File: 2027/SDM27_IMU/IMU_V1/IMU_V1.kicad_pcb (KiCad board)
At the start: 2 copper layers, 80 parts, among them IC3 ISM330DHCXTR, IC7 IIS2MDCTR, J1 WEIPU SA12 7PIN, J3 USB_C_Receptacle_USB2.0_16P, U2 ESP32-C5HR8, U3 TPS2121RUXR, U4 TPS62901RPJR, U5 SST26VF064B-104I_SM, U6 TLP175A_TPL,E, U7 USBLC6-2SC6, U8 TCAN3403DRBRQ1, Y3 CX1612DB48000D0FPJC1

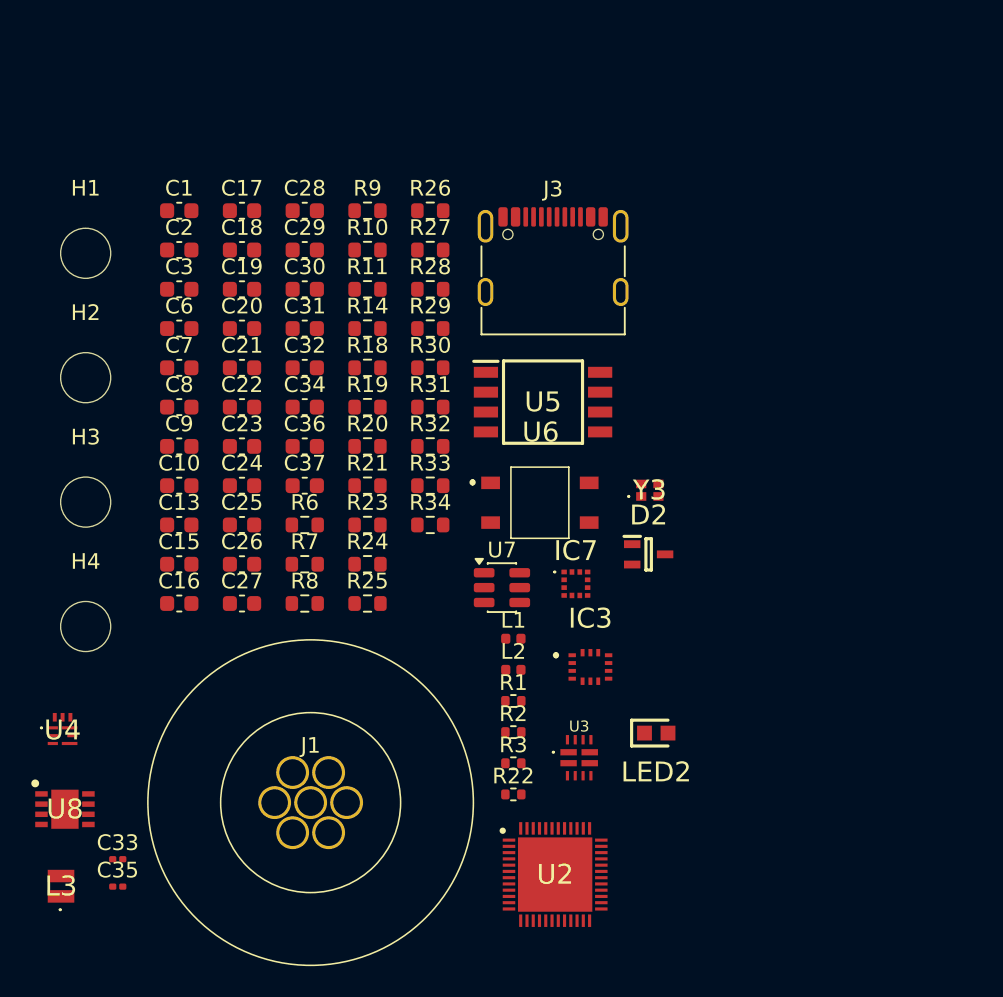
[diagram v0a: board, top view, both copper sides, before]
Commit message: IMU V1 Fixes
redesignated resistor and capacitor values to be sorted.
Added 7 pin jst-ph to board
Removed extra pair of resistors on USB D Pins that was added. (Already had a set on MCU)
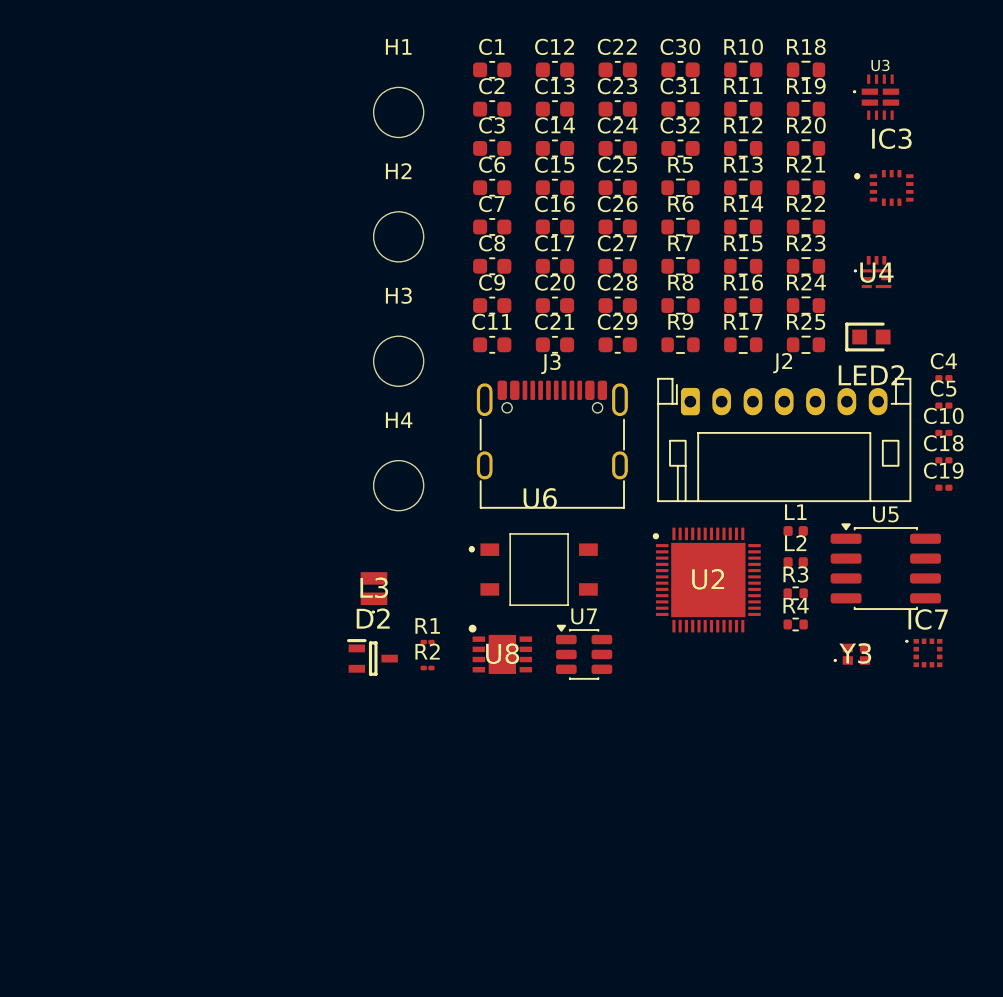
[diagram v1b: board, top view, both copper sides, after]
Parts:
- removed C33, C35: 12pF, Capacitor_SMD:C_0201_0603Metric
- removed C34, C36, C37: 100nF, Capacitor_SMD:C_0603_1608Metric
- removed J1: WEIPU SA12 7PIN, SDM Footprints:SA12 7Pin
- removed R26: 18.2k, Resistor_SMD:R_0603_1608Metric
- removed R27: 10.2k, Resistor_SMD:R_0603_1608Metric
- removed R28: 100k, Resistor_SMD:R_0603_1608Metric
- removed R29: 113k, Resistor_SMD:R_0603_1608Metric
- removed R30: 24.9k, Resistor_SMD:R_0603_1608Metric
- removed R31: 330, Resistor_SMD:R_0603_1608Metric
- removed R32, R33: 2.2k, Resistor_SMD:R_0603_1608Metric
- removed R34: 120, Resistor_SMD:R_0603_1608Metric
- added C11: 10uF, Capacitor_SMD:C_0603_1608Metric, F.Cu at (127.5, 93.8)
- added C12: 10uF, Capacitor_SMD:C_0603_1608Metric, F.Cu at (131.5, 76.3)
- added C14: 0.3pF, Capacitor_SMD:C_0603_1608Metric, F.Cu at (131.5, 81.3)
- added C4: 1uF, Capacitor_SMD:C_0201_0603Metric, F.Cu at (156.3, 96.0)
- added C5: 1uF, Capacitor_SMD:C_0201_0603Metric, F.Cu at (156.3, 97.7)
- added J2: Conn_01x07_Pin, Connector_JST:JST_PH_S7B-PH-K_1x07_P2.00mm_Horizontal, F.Cu at (140.1, 97.5)
- added R12: 18.2k, Resistor_SMD:R_0603_1608Metric, F.Cu at (143.5, 81.3)
- added R13: 5k, Resistor_SMD:R_0603_1608Metric, F.Cu at (143.5, 83.8)
- added R15: 23.7k, Resistor_SMD:R_0603_1608Metric, F.Cu at (143.5, 88.8)
- added R16: 10.2k, Resistor_SMD:R_0603_1608Metric, F.Cu at (143.5, 91.3)
- added R17: 5k, Resistor_SMD:R_0603_1608Metric, F.Cu at (143.5, 93.8)
- added R4: 27, Resistor_SMD:R_0402_1005Metric, F.Cu at (146.8, 111.7)
- added R5: 2.2k, Resistor_SMD:R_0603_1608Metric, F.Cu at (139.5, 83.8)
- C10: value 10uF -> 100nF; footprint Capacitor_SMD:C_0603_1608Metric -> Capacitor_SMD:C_0201_0603Metric
- C13: value 0.3pF -> 10uF
- C15: value 220nF -> 0.8pF
- C16: value 10uF -> 2.6pF
- C17: value 100nF -> 3pF
- C18, C19: value 100nF -> 12pF; footprint Capacitor_SMD:C_0603_1608Metric -> Capacitor_SMD:C_0201_0603Metric
- C20: value 1uF 10V 0603 -> 100nF
- C21: value 10uF 25V -> 100nF
- C22: value 10nF -> 100nF
- C23: value 22uF -> 100nF
- C24: value 0.8pF -> 100nF
- C25: value 10uF -> 1uF 10V 0603
- C26: value 100nF -> 10uF 25V
- C27: value 100nF -> 10nF
- C28: value 3pF -> 22uF
- C29: value 100nF -> 220nF
- C30: value 2.6pF -> 10uF
- C32: value 10uF -> 100nF
- C7, C8: value 1uF -> 100nF
- R1, R2: footprint Resistor_SMD:R_0402_1005Metric -> Resistor_SMD:R_01005_0402Metric
- R10: value 27 -> 100
- R11: value 27 -> 63.4k
- R14: value 63.4k -> 5k
- R18: value 10k -> 5k
- R19: value 2.2k -> 100k
- R20: value 2.2k -> 113k
- R21: value 5.1k -> 24.9k
- R22: value 27 -> 330; footprint Resistor_SMD:R_0402_1005Metric -> Resistor_SMD:R_0603_1608Metric
- R23: value 5.1k -> 10k
- R24: value 23.7k -> 2.2k
- R25: value 5k -> 2.2k
- R6: value 10k -> 2.2k
- R7: value 5k -> 10k
- R8, R9: value 5k -> 5.1k
- U5: value SST26VF064B-104I_SM -> GD25Q32ESIG; footprint SDM Footprints:SOIC127P794X203-8N -> Package_SO:SOP-8_3.76x4.96mm_P1.27mm
- moved U4 59.6 mm to (152.0, 89.3)
- moved C10 49.0 mm to (156.3, 99.5)
- moved C18 46.8 mm to (156.3, 101.2)
- moved C19 46.6 mm to (156.3, 103.0)
- moved U3 46.4 mm to (152.3, 78.0)
- moved R22 40.8 mm to (147.5, 86.3)
- moved IC3 36.2 mm to (153.0, 83.8)
- moved C13 35.8 mm to (131.5, 78.8)
- moved C15 34.0 mm to (131.5, 83.8)
- moved C16 34.0 mm to (131.5, 86.3)
- moved R18 33.9 mm to (147.5, 76.3)
- moved R19 33.9 mm to (147.5, 78.8)
- moved R21 33.9 mm to (147.5, 83.8)
- moved R20 33.9 mm to (147.5, 81.3)
- moved R24 32.5 mm to (147.5, 91.3)
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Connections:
- C10 pad 1: +3.3V -> /VDD_SPI
- C15 pad 1: Net-(IC7-C1) -> +3.3V
- C16 pad 1: +3.3V -> Net-(U2-VDDA1)
- C18 pad 1: +3.3V -> Net-(C18-Pad1)
- C18 pad 2: GND -> Net-(C18-Pad2)
- C19 pad 1: GND -> Net-(U2-XTAL_N)
- C19 pad 2: VBUS -> Net-(C19-Pad2)
- C20 pad 1: Net-(U3-SS) -> GND
- C20 pad 2: GND -> +3.3V
- C21 pad 1: VCC -> GND
- C21 pad 2: GND -> +3.3V
- C22 pad 1: Net-(U4-SS/TR) -> GND
- C22 pad 2: GND -> VBUS
- C25 pad 1: +3.3V -> Net-(U3-SS)
- C26 pad 1: +3.3V -> VCC
- C27 pad 1: +3.3V -> Net-(U4-SS/TR)
- C29 pad 1: +3.3V -> Net-(IC7-C1)
- C30 pad 1: Net-(U2-VDDA1) -> +3.3V
- C6 pad 1: GND -> +3.3V
- C6 pad 2: +3.3V -> GND
- C7 pad 1: /CHIP_PU -> +3.3V
- C8 pad 1: Net-(U2-BOOT) -> +3.3V
- C9 pad 1: GND -> +3.3V
- C9 pad 2: +3.3V -> GND
- IC3 pad 12: Net-(IC3-CS) -> /I_CS
- IC7 pad 3: Net-(IC7-CS) -> /M_CS
- J3 pad A12: unconnected-(J3-GND-PadA12) -> GND
- J3 pad B1: unconnected-(J3-GND-PadB1) -> GND
- J3 pad B12: unconnected-(J3-GND-PadB12) -> GND
- L1 pad 2: Net-(C33-Pad1) -> Net-(C18-Pad1)
- R10 pad 1: /USB_D+ -> Net-(R10-Pad1)
- R10 pad 2: Net-(R10-Pad2) -> /CAN+
- R11 pad 1: /USB_D- -> Net-(U3-OV1)
- R11 pad 2: Net-(R11-Pad2) -> +12V
- R14 pad 1: Net-(U3-OV1) -> GND
- R14 pad 2: +12V -> Net-(U3-OV1)
- R18 pad 1: +3.3V -> GND
- R18 pad 2: Net-(IC7-CS) -> Net-(U3-OV2)
- R19 pad 1: /SDX -> GND
- R19 pad 2: +3.3V -> Net-(U3-ILIM)
- R20 pad 2: /SCX -> Net-(U4-VSET)
- R21 pad 1: Net-(J3-CC1) -> Net-(U4-VSET)
- R22 pad 1: /USB_D- -> +3.3V
- R22 pad 2: Net-(U2-GPIO13) -> /PWR_LED
- R23 pad 1: Net-(J3-CC2) -> +3.3V
- R23 pad 2: GND -> /M_CS
- R24 pad 1: Net-(U3-OV2) -> /SDX
- R24 pad 2: VBUS -> +3.3V
- R25 pad 1: GND -> +3.3V
- R25 pad 2: Net-(U3-OV2) -> /SCX
- R6 pad 1: Net-(IC3-CS) -> /I2C1_SCL
- R7 pad 1: GND -> /I_CS
- R7 pad 2: Net-(U3-PR1) -> +3.3V
- R8 pad 1: GND -> Net-(J3-CC1)
- R8 pad 2: Net-(U3-OV1) -> GND
- R9 pad 1: GND -> Net-(J3-CC2)
- R9 pad 2: Net-(U3-CP2) -> GND
- U2 pad 10: unconnected-(U2-GPIO1-Pad10) -> /I_CS
- U2 pad 11: unconnected-(U2-GPIO2-Pad11) -> /M_CS
- U6 pad 6: Net-(R34-Pad1) -> Net-(R10-Pad1)
- U7 pad 1: Net-(R10-Pad2) -> /USB_D+
- U7 pad 3: Net-(R11-Pad2) -> /USB_D-
- Y3 pad 1: Net-(C33-Pad2) -> Net-(C18-Pad2)
- Y3 pad 3: Net-(C35-Pad2) -> Net-(C19-Pad2)

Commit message: port to pc
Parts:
- removed J2: Conn_01x07_Pin, Connector_JST:JST_PH_S7B-PH-K_1x07_P2.00mm_Horizontal
- added J1: WEIPU SA12 7PIN, Connector_JST:JST_PH_B7B-PH-K_1x07_P2.00mm_Vertical, F.Cu at (145.0, 151.5)
- added SW1: SW_Push, Button_Switch_SMD:SW_SPST_CK_KXT3, F.Cu at (131.0, 161.5)
- added SW2: SW_Push, Button_Switch_SMD:SW_SPST_CK_KXT3, F.Cu at (131.0, 166.0)
- moved H1 86.9 mm to (178.0, 145.0)
- moved H2 82.7 mm to (168.5, 155.0)
- moved U3 73.7 mm to (101.5, 131.5), turned to -90 degrees
- moved L1 63.5 mm to (207.0, 85.2)
- moved L2 63.5 mm to (207.0, 87.2)
- moved R3 63.5 mm to (207.0, 89.2)
- moved R4 63.5 mm to (207.0, 91.2)
- moved H4 63.2 mm to (169.0, 144.5)
- moved U4 61.7 mm to (107.1, 131.8), turned to 180 degrees
- moved H3 61.5 mm to (168.5, 134.5)
- moved LED2 60.7 mm to (107.5, 135.0)
- moved R1 58.7 mm to (178.8, 93.5)
- moved R2 58.7 mm to (178.8, 95.2)
- moved C1 56.0 mm to (183.5, 77.3)
- moved C11 56.0 mm to (183.5, 94.8)
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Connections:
- net /CHIP_PU renamed /CP
- net Net-(U2-BOOT) renamed /BOOT
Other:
- board outline added: 52 x 41 mm
- copper layers 2 -> 4
- board text added: "BUCK"
- board text added: "CAN D2"
- board text added: "CRY"
- board text added: "ESD (U7)"
- board text added: "ESP-C5"
- board text added: "FLASH"
- board text added: "IMU"
- board text added: "JST"
- board text added: "LED"
- board text added: "MAG"
- board text added: "MUX"
- board text added: "OPTO"
- board text added: "Switch"
- board text added: "TCAN"
- board text added: "USB"
- board text added: "temp"

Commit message: IMU PCB V1
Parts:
- C1, C12, C16, C17, C18, C19, C2, C7, C8, J3, L1, L2, Y3: moved to B.Cu
- moved H1 85.0 mm to (115.0, 88.0)
- moved R3 81.8 mm to (126.5, 104.0), turned to 180 degrees
- moved R4 81.2 mm to (126.5, 102.1)
- moved R18 76.8 mm to (131.7, 104.5), turned to -90 degrees
- moved R9 76.4 mm to (121.5, 114.0), turned to 180 degrees
- moved R11 76.2 mm to (129.7, 110.5), turned to -90 degrees
- moved C22 76.1 mm to (123.0, 110.5)
- moved R12 73.9 mm to (131.2, 110.5), turned to -90 degrees
- moved R8 73.7 mm to (125.0, 114.0)
- moved L2 73.3 mm to (134.6, 98.9), turned to 90 degrees
- moved R14 72.6 mm to (129.7, 107.5), turned to -90 degrees
- moved R19 72.0 mm to (137.7, 109.0), turned to 90 degrees
- moved R13 71.9 mm to (131.2, 107.5), turned to -90 degrees
- moved C10 71.6 mm to (130.1, 94.3), turned to 180 degrees
- moved SW1 69.4 mm to (115.0, 94.0)
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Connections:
- U2 pad 10: /I_CS -> unconnected-(U2-GPIO1-Pad10)
- U2 pad 11: /M_CS -> unconnected-(U2-GPIO2-Pad11)
- U2 pad 13: unconnected-(U2-GPIO4-Pad13) -> /CAN_CTX
- U2 pad 14: unconnected-(U2-GPIO5-Pad14) -> /CAN_RTX
- U2 pad 16: unconnected-(U2-GPIO7-Pad16) -> /M_CS
- U2 pad 19: /CAN_TERM -> /I_CS
- U2 pad 20: unconnected-(U2-GPIO11-Pad20) -> /INT
- U2 pad 33: /CAN_CTX -> unconnected-(U2-GPIO23-Pad33)
- U2 pad 34: /CAN_RTX -> unconnected-(U2-GPIO24-Pad34)
- U2 pad 9: /INT -> unconnected-(U2-GPIO0-Pad9)
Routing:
- net GND: track 0.00 -> 90.5 mm, vias 0 -> 26
- net +3.3V: track 0.00 -> 52.0 mm, vias 0 -> 17
- net /CP: track 0.00 -> 41.2 mm, vias 0 -> 2
- net VBUS: track 0.00 -> 32.2 mm, vias 0 -> 6
- net /CAN-: track 0.00 -> 30.9 mm
- net /CAN+: track 0.00 -> 27.9 mm, vias 0 -> 2
- net /BOOT: track 0.00 -> 22.6 mm, vias 0 -> 2
- net /CAN_TERM: track 0.00 -> 20.8 mm
- net /INT: track 0.00 -> 19.4 mm, vias 0 -> 2
- net Net-(U2-GPIO13): track 0.00 -> 19.0 mm, vias 0 -> 2
- net Net-(U2-GPIO14): track 0.00 -> 18.9 mm, vias 0 -> 2
- net /CAN_RTX: track 0.00 -> 16.9 mm
- net /CAN_CTX: track 0.00 -> 16.6 mm
- net /SCX: track 0.00 -> 15.8 mm, vias 0 -> 2
- net /SDX: track 0.00 -> 14.5 mm, vias 0 -> 3
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- added copper zone on In2.Cu, net +3.3V
- added copper zone on In1.Cu, net GND
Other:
- board size 52 x 41 mm -> 45.8 x 32 mm

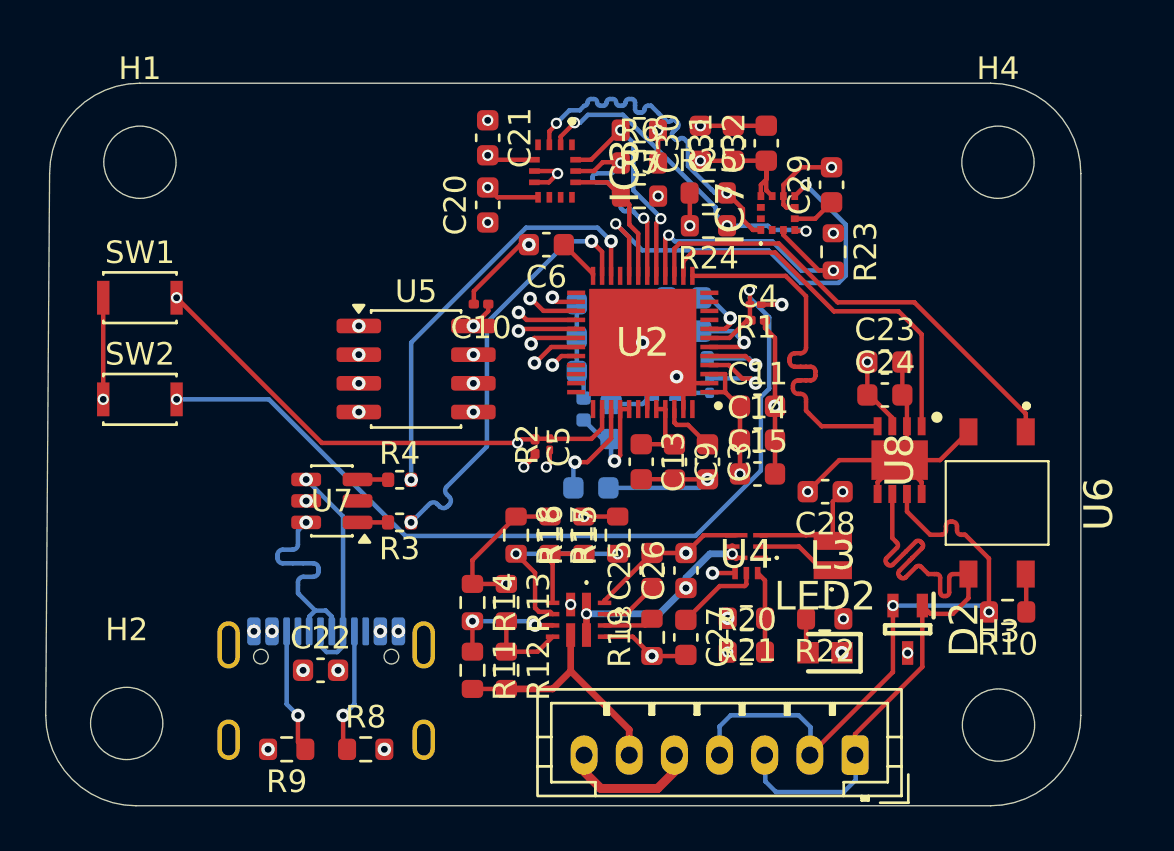
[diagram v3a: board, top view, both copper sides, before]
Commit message: IMU V1 Revisions
Components on 1 side
Revised Routing.
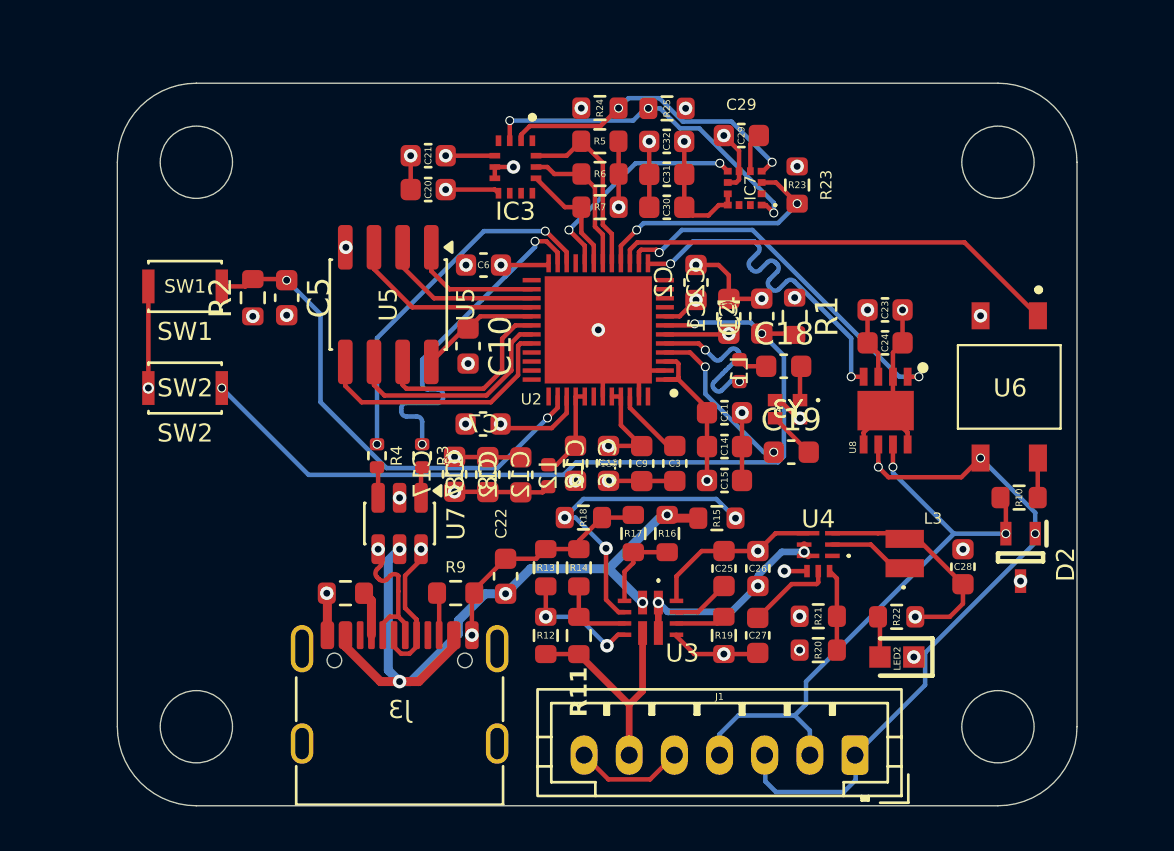
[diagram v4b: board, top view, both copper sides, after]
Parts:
- C1, C12, C16, C17, C2, C7, C8, J3, L1, L2, Y3: moved to F.Cu
- C10, C4, C5: footprint Capacitor_SMD:C_0201_0603Metric -> Capacitor_SMD:C_0603_1608Metric
- C18, C19: footprint Capacitor_SMD:C_0201_0603Metric -> Capacitor_SMD:C_0603_1608Metric; moved to F.Cu
- R1, R2: footprint Resistor_SMD:R_01005_0402Metric -> Resistor_SMD:R_0603_1608Metric
- moved R2 14.7 mm to (120.0, 94.0)
- moved C5 12.8 mm to (121.5, 94.0)
- moved R9 10.2 mm to (129.0, 107.1), turned to 0 degrees
- moved C22 9.19 mm to (131.2, 106.3), turned to -90 degrees
- moved C12 8.25 mm to (131.9, 101.8), turned to 90 degrees
- moved C8 7.69 mm to (130.4, 101.8), turned to 90 degrees
- moved C17 7.68 mm to (128.9, 101.8), turned to 90 degrees
- moved R24 7.09 mm to (135.4, 85.6)
- moved R8 6.97 mm to (124.1, 107.1), turned to 180 degrees
- moved C28 6.95 mm to (151.5, 105.9), turned to 90 degrees
- moved D2 5.93 mm to (154.0, 105.5)
- moved Y3 5.56 mm to (143.7, 98.9), turned to 180 degrees
- moved C7 5.55 mm to (130.2, 99.6), turned to 180 degrees
- moved C18 5.53 mm to (143.5, 97.0), turned to 0 degrees
- moved U6 5.17 mm to (153.5, 98.0)
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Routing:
- net GND: track 90.5 -> 71.9 mm, vias 26 -> 30
- net /INT: track 19.4 -> 10.2 mm
- net Net-(U3-OV2): track 8.14 -> 14.0 mm, vias 2 -> 3
- net /VDD_SPI: track 11.1 -> 5.28 mm, vias 2 -> 0
- net /SPICS0: track 11.1 -> 5.83 mm, vias 2 -> 0
- net /SPIQ: track 11.1 -> 7.16 mm, vias 2 -> 0
- net Net-(J3-CC2): track 5.57 -> 1.90 mm, vias 1 -> 0
- net Net-(J3-CC1): track 5.50 -> 1.99 mm, vias 1 -> 0
- net /I2C1_SCL: track 9.91 -> 6.48 mm, vias 2 -> 0
- net /USBM_D-: track 9.93 -> 6.59 mm
- net /USBM_D+: track 9.87 -> 6.59 mm
- net Net-(U2-GPIO14): track 18.9 -> 15.8 mm
- net Net-(U2-GPIO13): track 19.0 -> 15.9 mm
- net Net-(U2-XTAL_P): track 4.48 -> 7.29 mm, vias 1 -> 2
- net Net-(U2-XTAL_N): track 4.60 -> 7.35 mm, vias 1 -> 2
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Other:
- board size 45.8 x 32 mm -> 42.5 x 32 mm
- board text removed: "BUCK"
- board text removed: "CAN D2"
- board text removed: "CRY"
- board text removed: "ESD (U7)"
- board text removed: "ESP-C5"
- board text removed: "FLASH"
- board text removed: "IMU"
- board text removed: "JST"
- board text removed: "LED"
- board text removed: "MAG"
- board text removed: "MUX"
- board text removed: "OPTO"
- board text removed: "Switch"
- board text removed: "TCAN"
- board text removed: "USB"
- board text removed: "temp"
